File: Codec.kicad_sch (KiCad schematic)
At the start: 2 parts, among them U2 TLV320AIC3104IRHBR, U3 TLV320AIC3104IRHBR

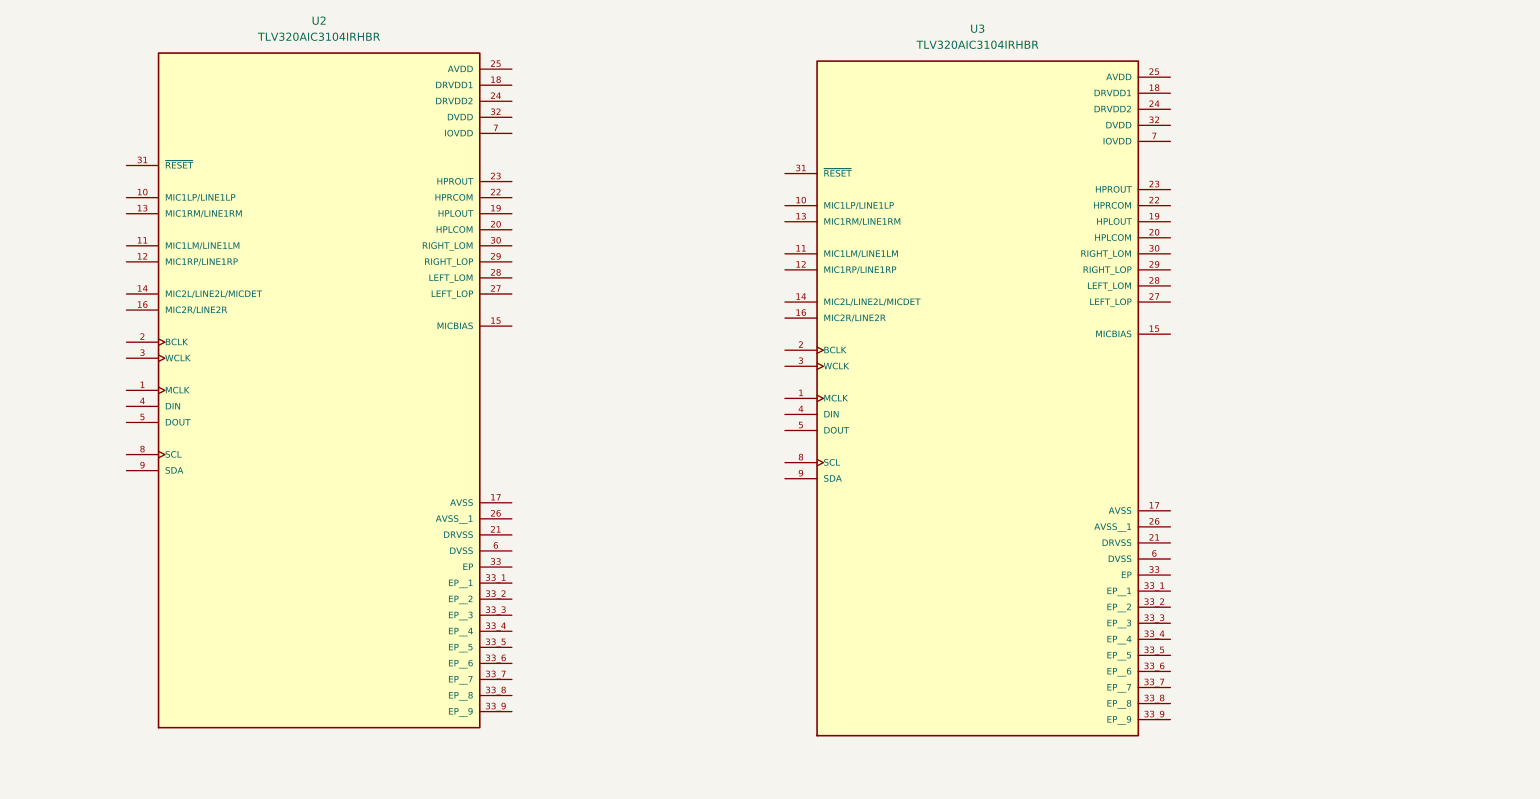
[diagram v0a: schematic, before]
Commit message: MOD : KiCad 8.0.1 -> 9.0.0. ADD : Codec power circuitry.
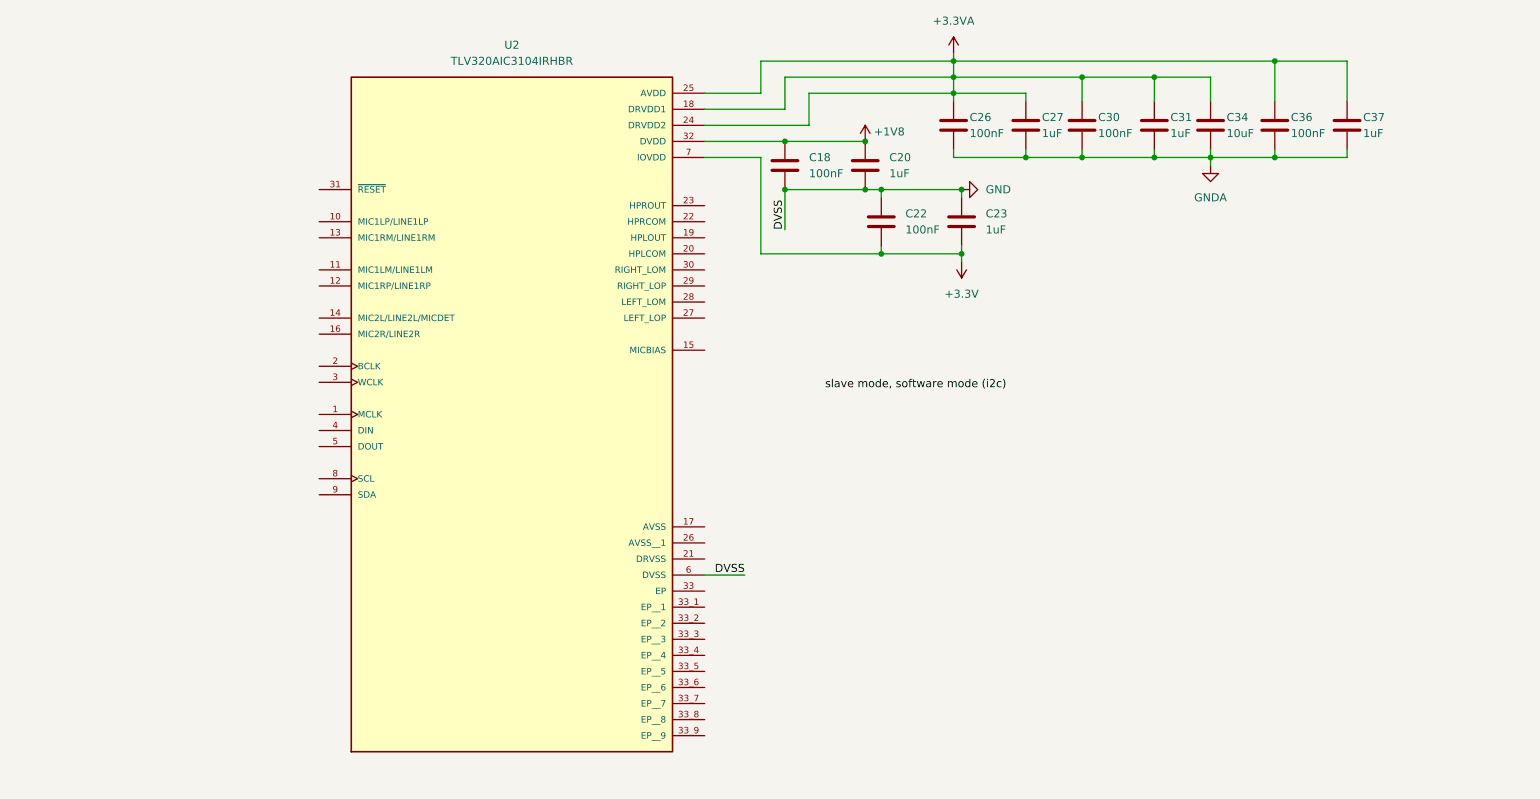
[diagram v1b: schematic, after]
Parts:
- removed U3: TLV320AIC3104IRHBR, TLV320AIC3104IRHBR:QFN50P500X500X100-33N, symbol TLV320AIC3104IRHBR:TLV320AIC3104IRHBR
- added C18, C22, C26, C30, C36: 100nF, symbol Device:C
- added C20, C23, C27, C31, C37: 1uF, symbol Device:C
- added C34: 10uF, symbol Device:C
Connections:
- net +3.3VA: now reaches U2.18 (DRVDD1)
- net +3.3VA: now also U2.24 (DRVDD2), U2.25 (AVDD), C26.2, C27.2, C30.2, C31.2, C34.2, C36.2, C37.2
- net +1V8: now reaches U2.32 (DVDD)
- net +1V8: now also C18.2, C20.2
- net GND: now reaches U2.6 (DVSS)
- net GND: now also C18.1, C20.1, C22.2, C23.2
- net +3.3V: now reaches U2.7 (IOVDD)
- net +3.3V: now also C22.1, C23.1
- new net GNDA: C26.1, C27.1, C30.1, C31.1, C34.1, C36.1, C37.1
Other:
- moved on the sheet: U2

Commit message: ADD : Finished codec power and data connections
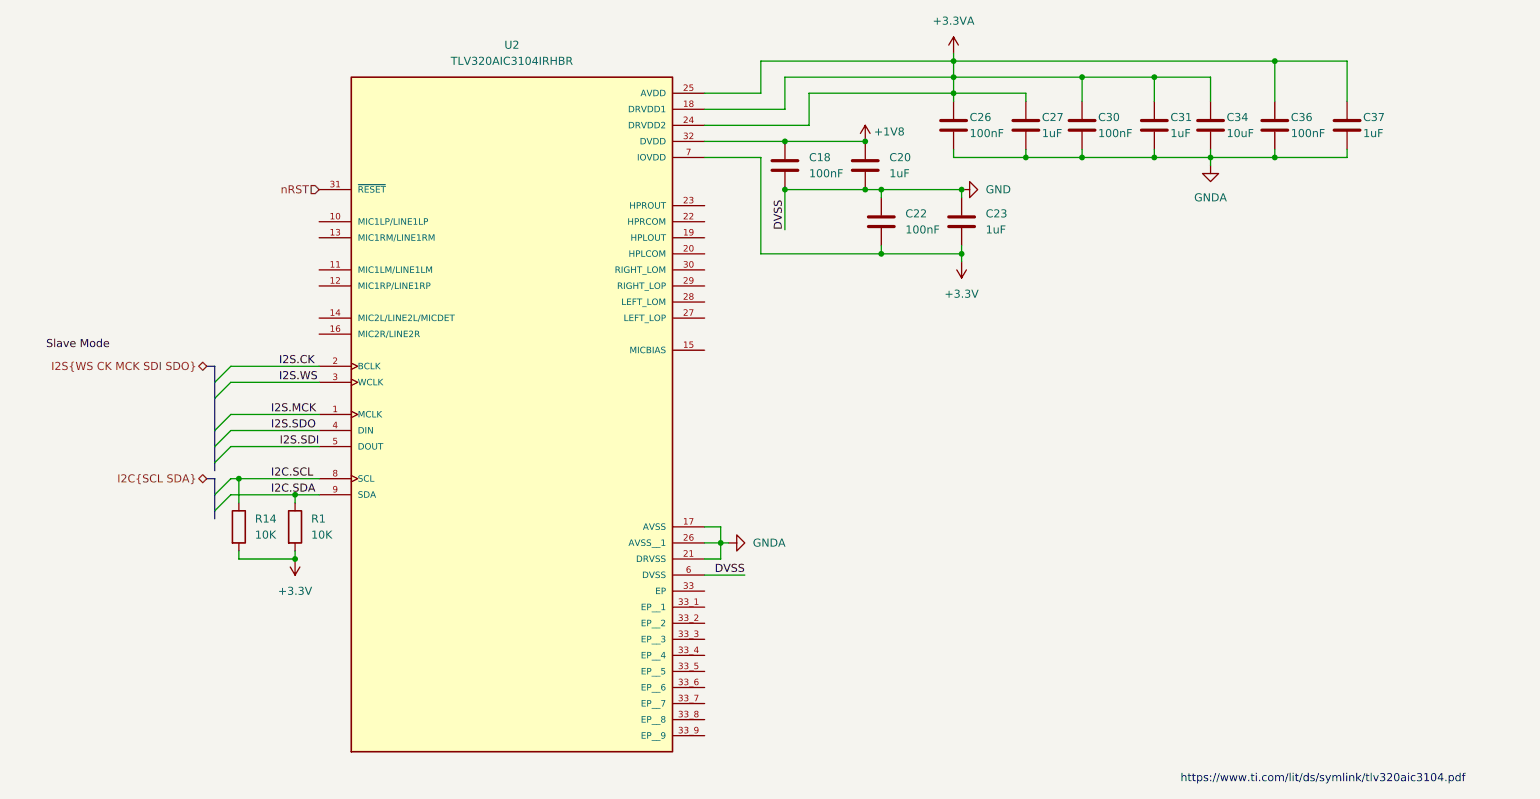
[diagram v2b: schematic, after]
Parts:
- added R1, R14: 10K, symbol Device:R
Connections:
- net +3.3V: now also R1.2, R14.2
- net GNDA: now also U2.17 (AVSS), U2.21 (DRVSS), U2.26 (AVSS__1)
- net I2S.MCK: now reaches U2.1 (MCLK)
- net I2S.CK: now reaches U2.2 (BCLK)
- net I2S.WS: now reaches U2.3 (WCLK)
- net nRST: now reaches U2.31 (~{RESET})
- net I2S.SDO: now reaches U2.4 (DIN)
- net I2S.SDI: now reaches U2.5 (DOUT)
- net I2C.SCL: now reaches U2.8 (SCL)
- net I2C.SCL: now also R14.1
- net I2C.SDA: now reaches U2.9 (SDA)
- net I2C.SDA: now also R1.1
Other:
- note added: "https://www.ti.com/lit/ds/symlink/tlv320aic3104.pdf"

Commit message: ADD : Footprint assignment. FIX : Various ERC rules.
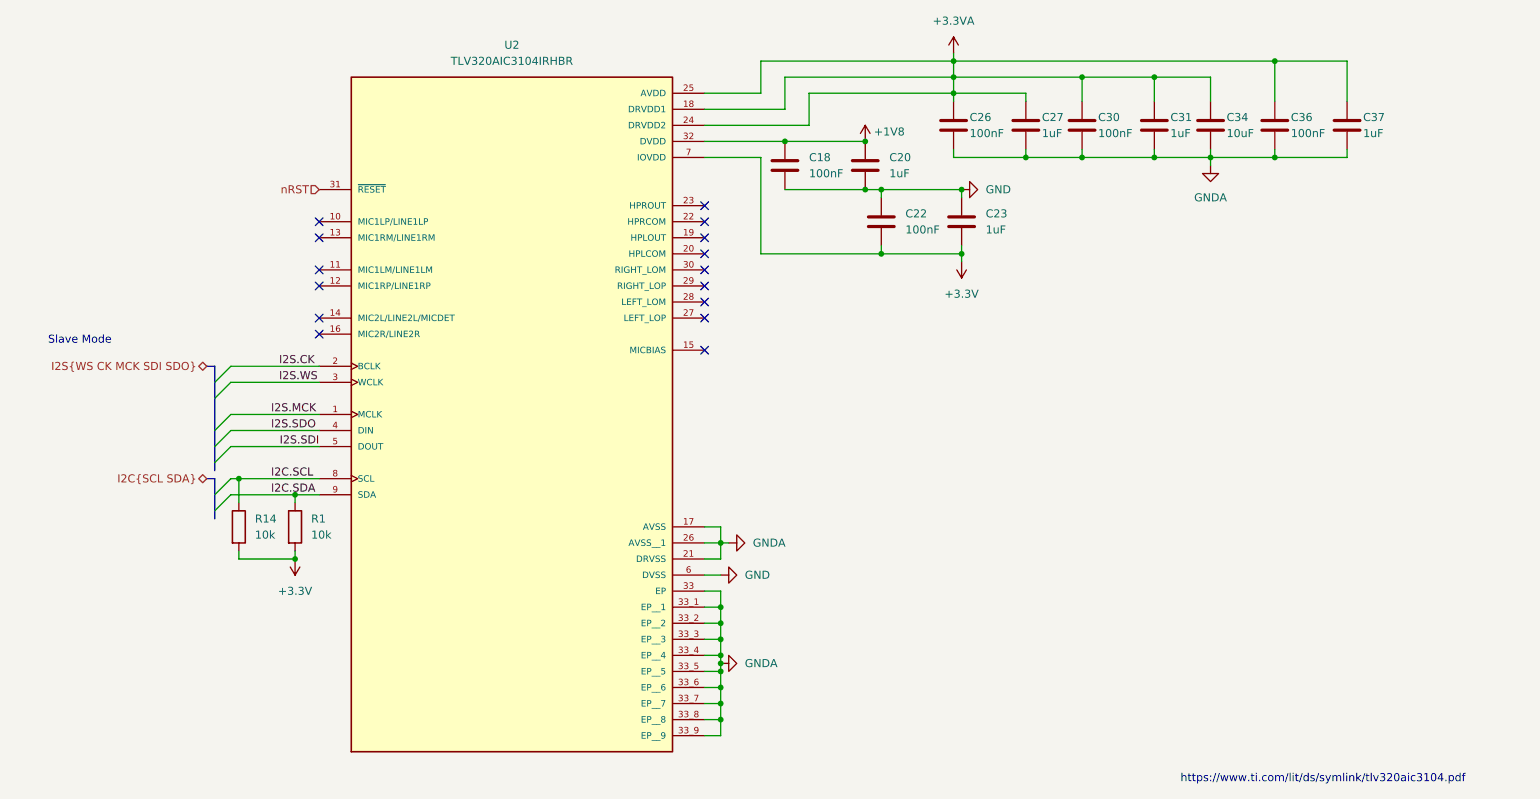
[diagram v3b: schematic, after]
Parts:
- C18, C20, C22, C23, C26, C27, C30, C31, C34, C36, C37: footprint (none) -> Capacitor_SMD:C_0402_1005Metric
- R1, R14: value 10K -> 10k; footprint (none) -> Resistor_SMD:R_0402_1005Metric
- U2: footprint TLV320AIC3104IRHBR:QFN50P500X500X100-33N -> random-footprints:QFN50P500X500X100-33N
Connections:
- net GNDA: now also U2.33 (EP), U2.33_1 (EP__1), U2.33_2 (EP__2), U2.33_3 (EP__3), U2.33_4 (EP__4), U2.33_5 (EP__5), U2.33_6 (EP__6), U2.33_7 (EP__7), U2.33_8 (EP__8), U2.33_9 (EP__9)
- no-connect marks 0 -> 15
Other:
- note added: "Slave Mode"
